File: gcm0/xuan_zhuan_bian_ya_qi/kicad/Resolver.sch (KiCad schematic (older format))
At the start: 85 parts, among them U1 L7805, U2 LM1117-3.3, U3 74HC595, U4 STM32F030F4Px, Y1 8MHZ

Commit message: 电路图改错
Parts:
- R1, R2, R3: value R -> 10K
- R5, R6: value R -> 1K
- gave numbers to parts that had none: 56
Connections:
- wire segments 241 -> 242
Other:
- note added: "LCD"
- moved on the sheet: C1, C10, C11, C12, C13, C14, C15, C16, C17, C18, C19, C2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

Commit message: 相位补偿
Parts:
- C20: value 104 -> 102
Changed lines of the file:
@@
 P 7400 5400
 F 0 "C20" H 7515 5446 50  0000 L CNN
-F 1 "104" H 7515 5355 50  0000 L CNN
+F 1 "102" H 7515 5355 50  0000 L CNN
 F 2 "" H 7438 5250 50  0001 C CNN
 F 3 "~" H 7400 5400 50  0001 C CNN

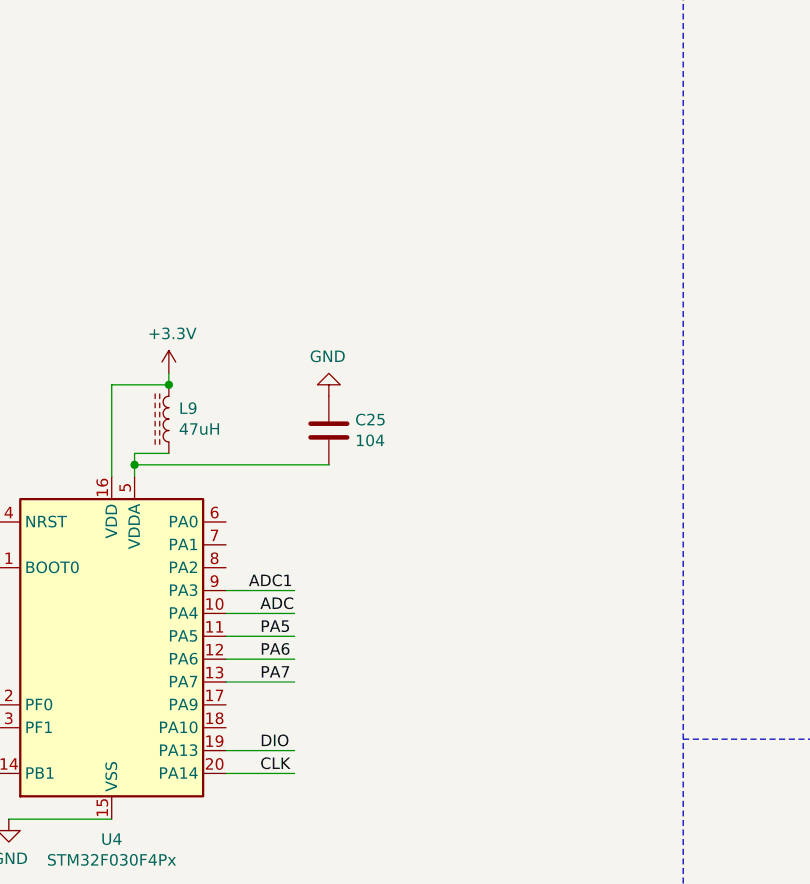
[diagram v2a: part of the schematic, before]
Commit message: 相位补偿成功
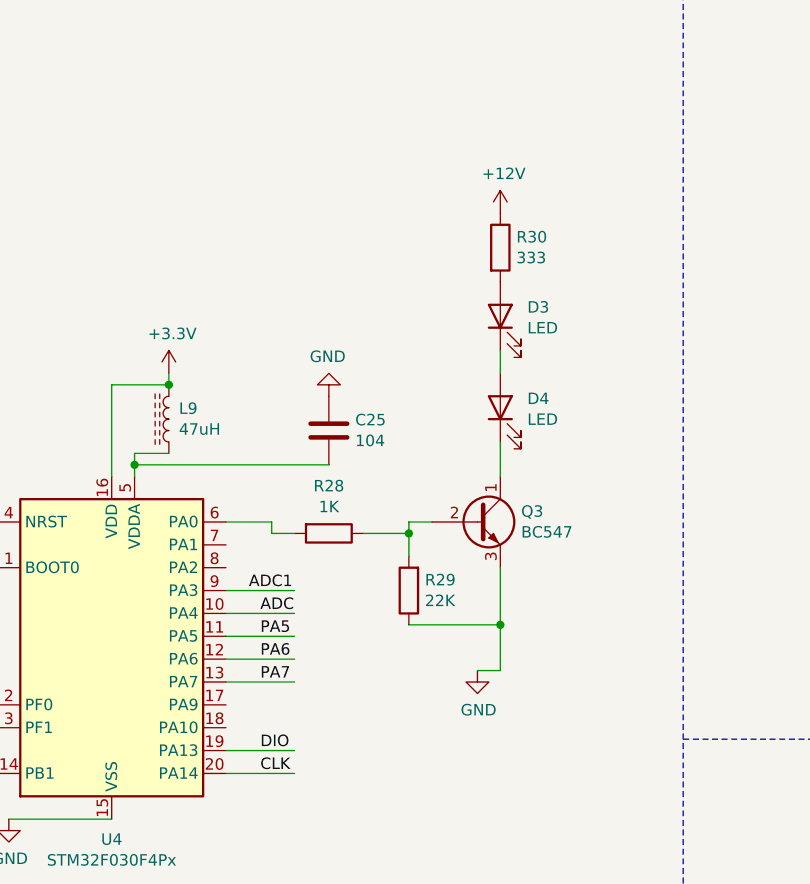
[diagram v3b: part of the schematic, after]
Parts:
- added D3, D4: LED, symbol Device:LED
- added Q3: BC547, Package_TO_SOT_THT:TO-92_Inline, symbol Transistor_BJT:BC547
- added R28: 1K, symbol Device:R
- added R29: 22K, symbol Device:R
- added R30: 333, symbol Device:R
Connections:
- wire segments 242 -> 255
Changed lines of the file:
@@
 Text Notes 7200 7950 0    236  ~ 47
 LCD
+$Comp
+L Transistor_BJT:BC547 Q3
+U 1 1 60251978
+P 10000 3900
+F 0 "Q3" H 10191 3946 50  0000 L CNN
+F 1 "BC547" H 10191 3855 50  0000 L CNN
+F 2 "Package_TO_SOT_THT:TO-92_Inline" H 10200 3825 50  0001 L CIN
+F 3 "https://www.onsemi.com/pub/Collateral/BC550-D.pdf" H 10000 3900 50  0001 L CNN
+	1    10000 3900
+	1    0    0    -1
+$EndComp
+$Comp
+L Device:R R28
+U 1 1 60256053
+P 9350 3950
+F 0 "R28" V 9143 3950 50  0000 C CNN
+F 1 "1K" V 9234 3950 50  0000 C CNN
+F 2 "" V 9280 3950 50  0001 C CNN
+F 3 "~" H 9350 3950 50  0001 C CNN
+	1    9350 3950
+	0    1    1    0
+$EndComp
+$Comp
+L Device:R R29
+U 1 1 60257B01
+P 9700 4200
+F 0 "R29" H 9630 4154 50  0000 R CNN
+F 1 "22K" H 9630 4245 50  0000 R CNN
+F 2 "" V 9630 4200 50  0001 C CNN
+F 3 "~" H 9700 4200 50  0001 C CNN
+	1    9700 4200
+	-1   0    0    1
+$EndComp
+$Comp
+L power:GND #PWR022
+U 1 1 60258EDE
+P 10000 4550
+F 0 "#PWR022" H 10000 4300 50  0001 C CNN
+F 1 "GND" H 10005 4377 50  0000 C CNN
+F 2 "" H 10000 4550 50  0001 C CNN
+F 3 "" H 10000 4550 50  0001 C CNN
+	1    10000 4550
+	1    0    0    -1
+$EndComp
+Wire Wire Line
+	10100 4100 10100 4350
+Wire Wire Line
+	10100 4550 10000 4550
+Wire Wire Line
+	9700 4350 10100 4350
+Connection ~ 10100 4350
+Wire Wire Line
+	10100 4350 10100 4550
+Wire Wire Line
+	9700 4050 9700 3950
+Wire Wire Line
+	9700 3950 9500 3950
+Wire Wire Line
+	9800 3900 9700 3900
+Wire Wire Line
+	9700 3900 9700 3950
+Connection ~ 9700 3950
+Wire Wire Line
+	9200 3950 9100 3950
+Wire Wire Line
+	9100 3950 9100 3900
+Wire Wire Line
+	9100 3900 8900 3900
+$Comp
+L Device:LED D4
+U 1 1 602B2D6F
+P 10100 3400
+F 0 "D4" V 10139 3282 50  0000 R CNN
+F 1 "LED" V 10048 3282 50  0000 R CNN
+F 2 "" H 10100 3400 50  0001 C CNN
+F 3 "~" H 10100 3400 50  0001 C CNN
+	1    10100 3400
+	0    -1   -1   0
+$EndComp
+$Comp
+L Device:LED D3
+U 1 1 602B4701
+P 10100 3000
+F 0 "D3" V 10139 2882 50  0000 R CNN
+F 1 "LED" V 10048 2882 50  0000 R CNN
+F 2 "" H 10100 3000 50  0001 C CNN
+F 3 "~" H 10100 3000 50  0001 C CNN
+	1    10100 3000
+	0    -1   -1   0
+$EndComp
+Wire Wire Line
+	10100 3250 10100 3150
+Wire Wire Line
+	10100 3550 10100 3700
+$Comp
+L power:+12V #PWR023
+U 1 1 602DB0C7
+P 10100 2550
+F 0 "#PWR023" H 10100 2400 50  0001 C CNN
+F 1 "+12V" H 10115 2723 50  0000 C CNN
+F 2 "" H 10100 2550 50  0001 C CNN
+F 3 "" H 10100 2550 50  0001 C CNN
+	1    10100 2550
+	1    0    0    -1
+$EndComp
+$Comp
+L Device:R R30
+U 1 1 602DDBDD
+P 10100 2700
+F 0 "R30" H 10170 2746 50  0000 L CNN
+F 1 "333" H 10170 2655 50  0000 L CNN
+F 2 "" V 10030 2700 50  0001 C CNN
+F 3 "~" H 10100 2700 50  0001 C CNN
+	1    10100 2700
+	1    0    0    -1
+$EndComp
 $EndSCHEMATC

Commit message: 1
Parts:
- renumbered D4 to D?, D3 to D?, Q3 to Q?, R28 to R?, R29 to R?, R30 to R?
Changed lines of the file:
@@
 LCD
 $Comp
-L Transistor_BJT:BC547 Q3
+L Transistor_BJT:BC547 Q?
 U 1 1 60251978
 P 10000 3900
-F 0 "Q3" H 10191 3946 50  0000 L CNN
+F 0 "Q?" H 10191 3946 50  0000 L CNN
 F 1 "BC547" H 10191 3855 50  0000 L CNN
 F 2 "Package_TO_SOT_THT:TO-92_Inline" H 10200 3825 50  0001 L CIN
@@
 $EndComp
 $Comp
-L Device:R R28
+L Device:R R?
 U 1 1 60256053
 P 9350 3950
-F 0 "R28" V 9143 3950 50  0000 C CNN
+F 0 "R?" V 9143 3950 50  0000 C CNN
 F 1 "1K" V 9234 3950 50  0000 C CNN
 F 2 "" V 9280 3950 50  0001 C CNN
@@
 $EndComp
 $Comp
-L Device:R R29
+L Device:R R?
 U 1 1 60257B01
 P 9700 4200
-F 0 "R29" H 9630 4154 50  0000 R CNN
+F 0 "R?" H 9630 4154 50  0000 R CNN
 F 1 "22K" H 9630 4245 50  0000 R CNN
 F 2 "" V 9630 4200 50  0001 C CNN
@@
 $EndComp
 $Comp
-L power:GND #PWR022
+L power:GND #PWR?
 U 1 1 60258EDE
 P 10000 4550
-F 0 "#PWR022" H 10000 4300 50  0001 C CNN
+F 0 "#PWR?" H 10000 4300 50  0001 C CNN
 F 1 "GND" H 10005 4377 50  0000 C CNN
 F 2 "" H 10000 4550 50  0001 C CNN
@@
 	9100 3900 8900 3900
 $Comp
-L Device:LED D4
+L Device:LED D?
 U 1 1 602B2D6F
 P 10100 3400
-F 0 "D4" V 10139 3282 50  0000 R CNN
+F 0 "D?" V 10139 3282 50  0000 R CNN
 F 1 "LED" V 10048 3282 50  0000 R CNN
 F 2 "" H 10100 3400 50  0001 C CNN
@@
 $EndComp
 $Comp
-L Device:LED D3
+L Device:LED D?
 U 1 1 602B4701
 P 10100 3000
-F 0 "D3" V 10139 2882 50  0000 R CNN
+F 0 "D?" V 10139 2882 50  0000 R CNN
 F 1 "LED" V 10048 2882 50  0000 R CNN
 F 2 "" H 10100 3000 50  0001 C CNN
@@
 	10100 3550 10100 3700
 $Comp
-L power:+12V #PWR023
+L power:+12V #PWR?
 U 1 1 602DB0C7
 P 10100 2550
-F 0 "#PWR023" H 10100 2400 50  0001 C CNN
+F 0 "#PWR?" H 10100 2400 50  0001 C CNN
 F 1 "+12V" H 10115 2723 50  0000 C CNN
 F 2 "" H 10100 2550 50  0001 C CNN
@@
 $EndComp
 $Comp
-L Device:R R30
+L Device:R R?
 U 1 1 602DDBDD
 P 10100 2700
-F 0 "R30" H 10170 2746 50  0000 L CNN
+F 0 "R?" H 10170 2746 50  0000 L CNN
 F 1 "333" H 10170 2655 50  0000 L CNN
 F 2 "" V 10030 2700 50  0001 C CNN
